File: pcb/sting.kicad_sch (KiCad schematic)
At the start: 100 parts, among them J1 Conn_01x02, SW1 SW_Push, SW10 SW_Push, SW11 SW_Push, SW12 SW_Push, SW13 SW_Push, SW14 SW_Push, SW15 SW_Push, SW16 SW_Push, SW17 SW_Push, SW18 SW_Push, SW19 SW_Push, SW2 SW_Push, SW20 SW_Push, SW21 RotaryEncoder_Switch, SW22 SW_Push, SW23 SW_Push, SW24 SW_Push, SW25 SW_Push, SW26 SW_Push, SW27 SW_Push, SW28 SW_Push, SW29 SW_Push, SW3 SW_Push, SW30 SW_Push, SW31 SW_Push, SW32 SW_Push, SW33 SW_Push, SW34 SW_Push, SW35 SW_Push, SW36 SW_Push, SW37 SW_Push, SW38 SW_Push, SW39 SW_Push, SW4 SW_Push, SW40 SW_Push, SW41 SW_Push, SW42 SW_Push, SW43 SW_Push, SW44 SW_Push, SW45 SW_Push, SW46 SW_Push, SW48 SW_Push, SW49 SW_Push, SW5 SW_Push, SW6 SW_Push, SW7 SW_Push, SW8 SW_Push, SW9 SW_Push, U1 nice_nano

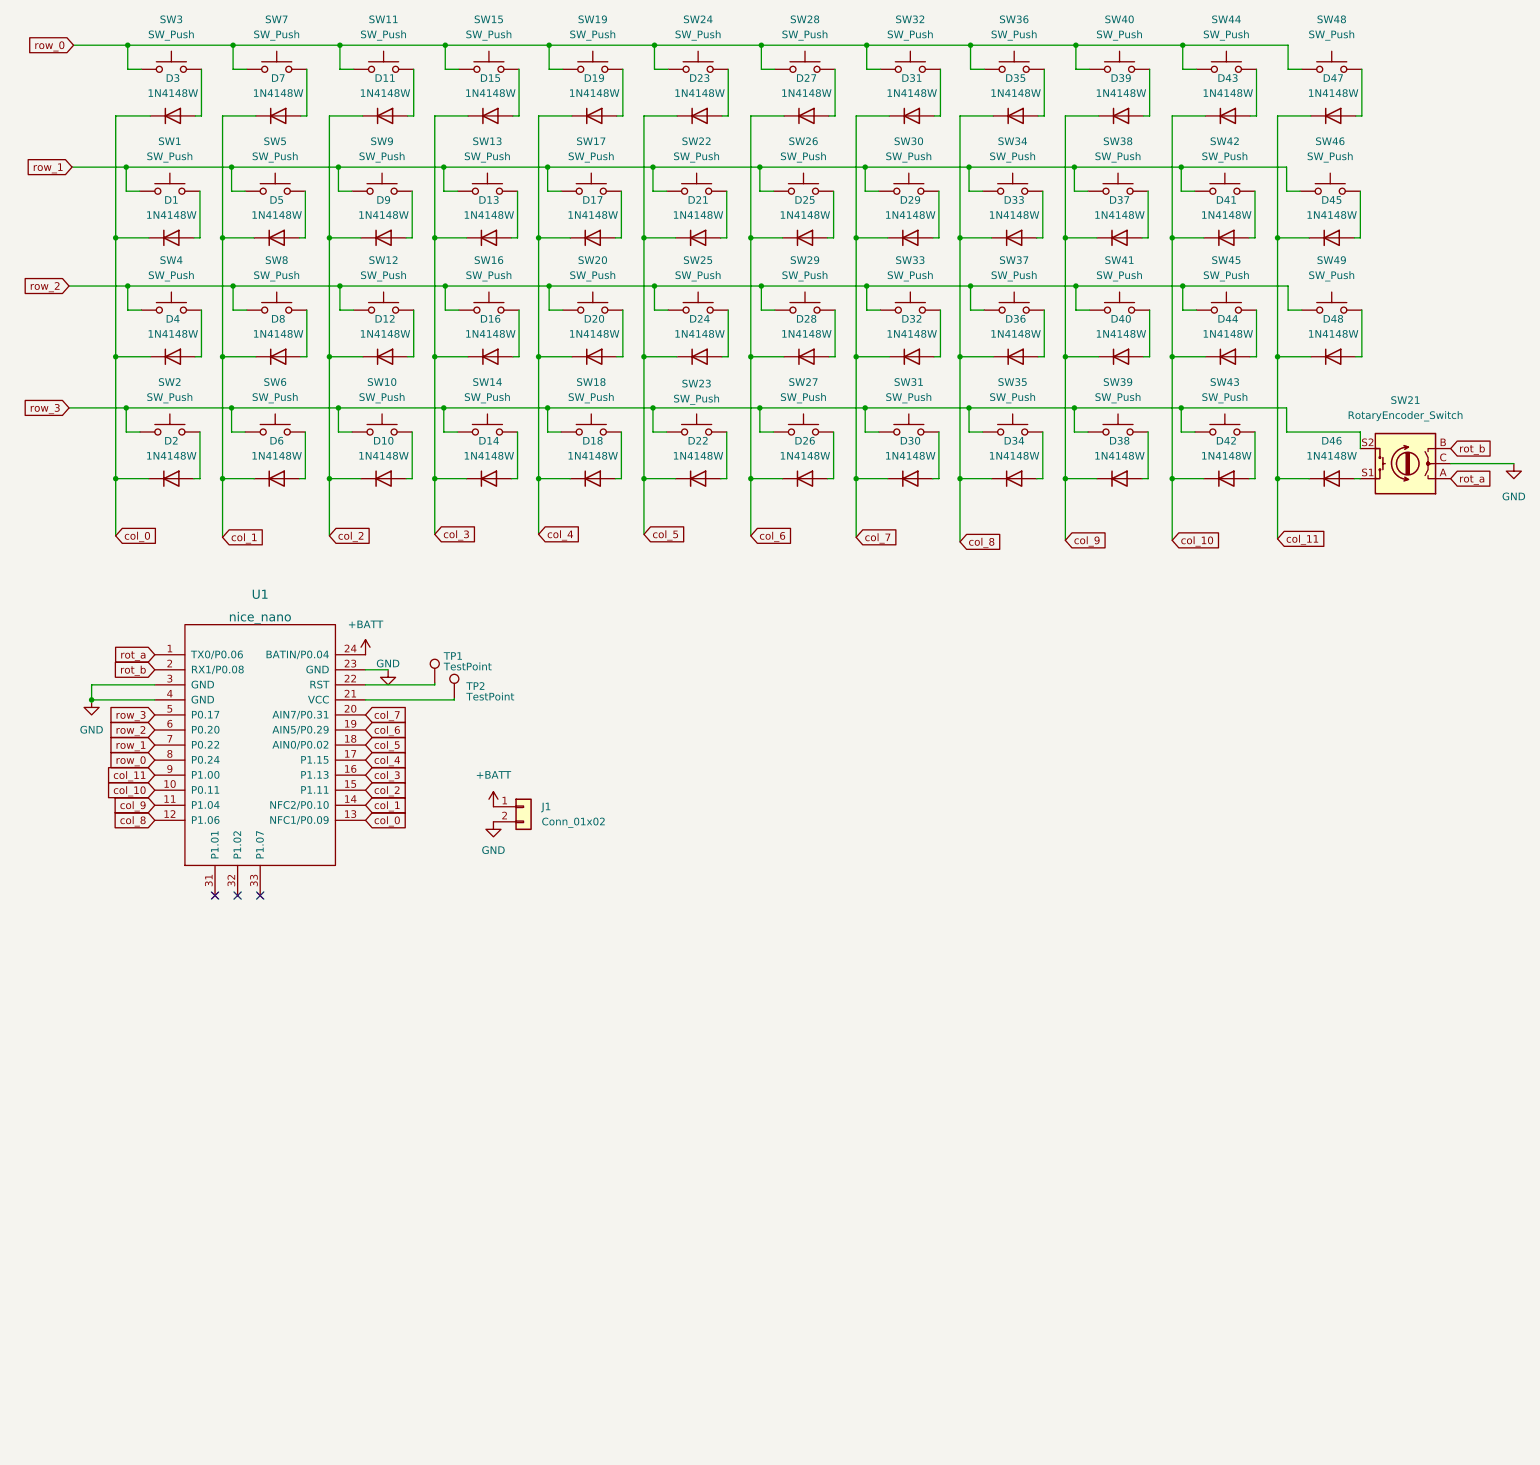
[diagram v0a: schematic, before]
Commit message: change key matrix and add encoder to schematic
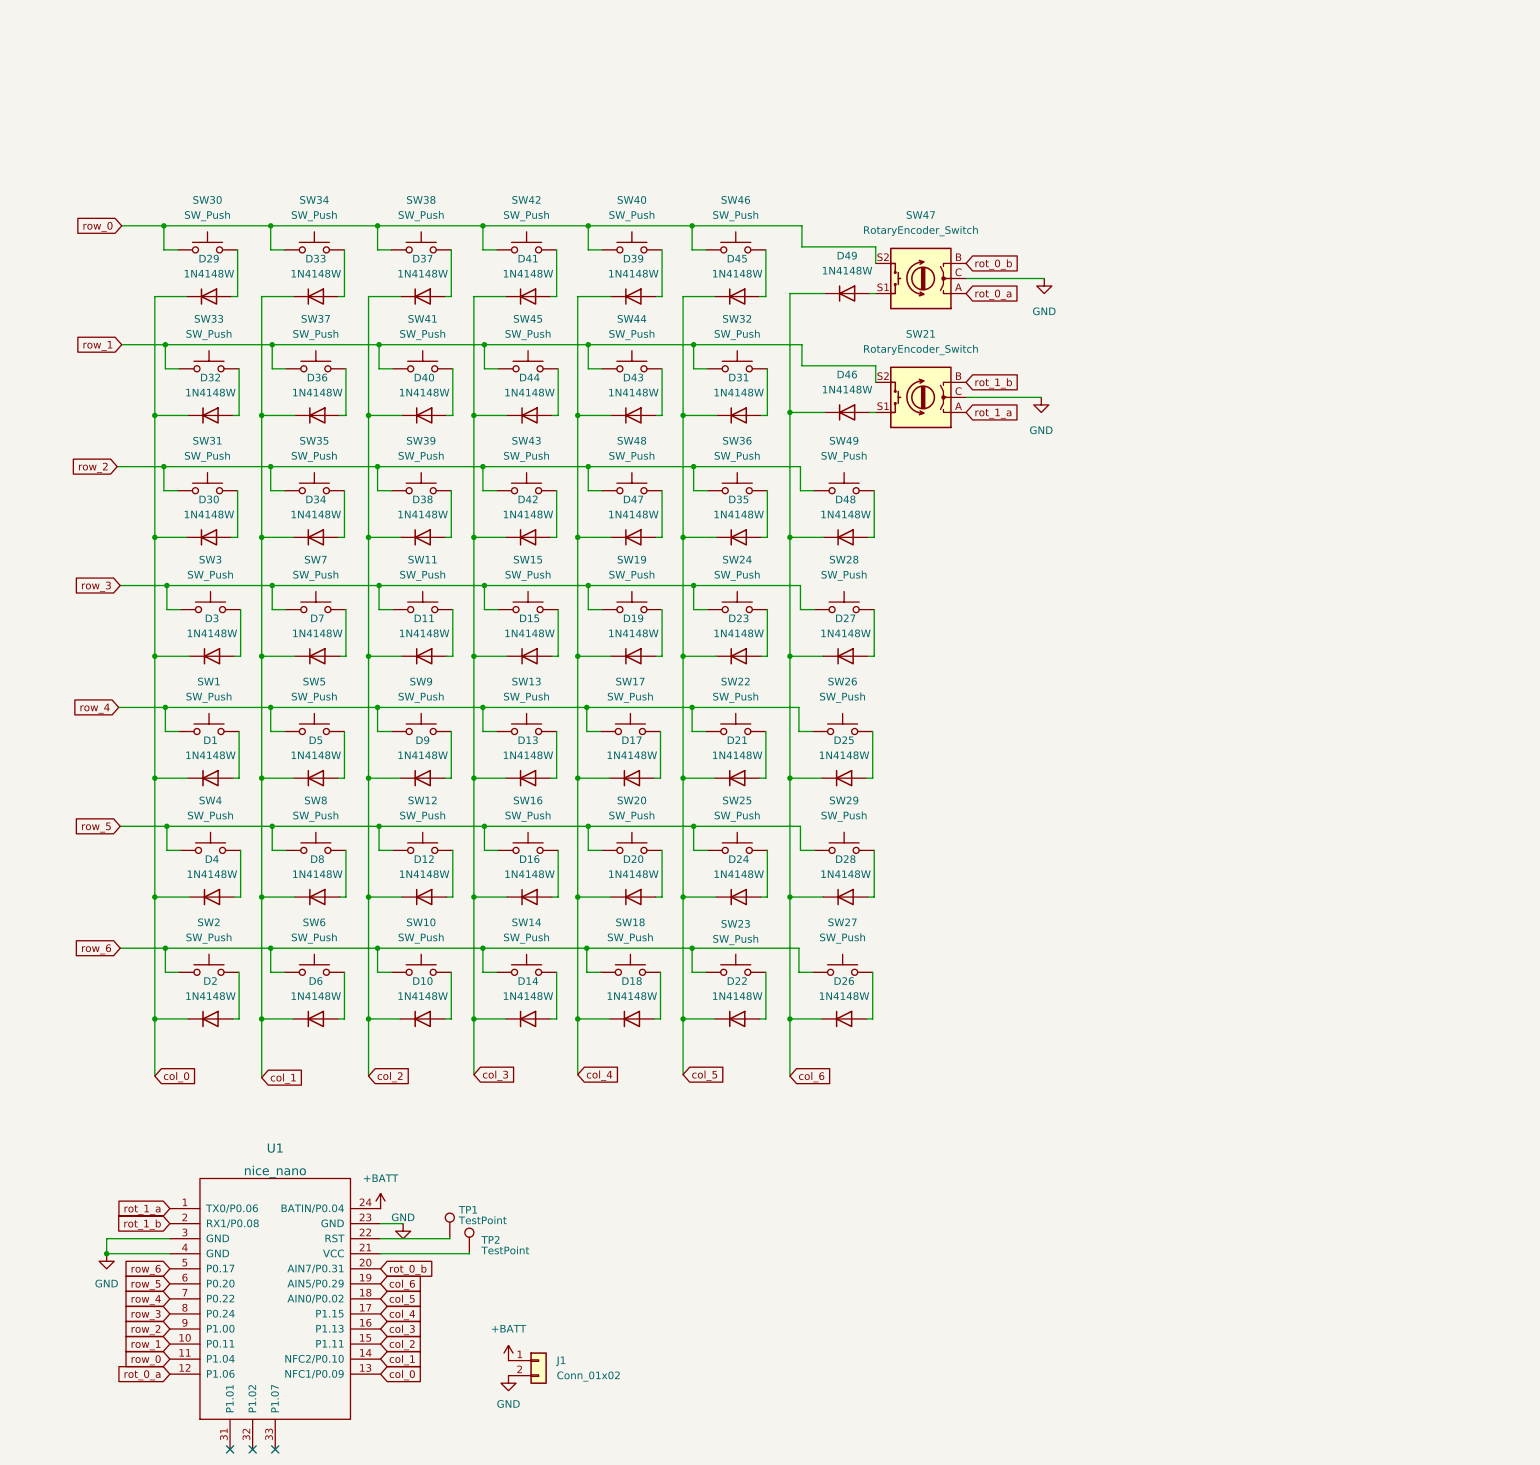
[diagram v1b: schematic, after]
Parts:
- added D49: 1N4148W, Diode_SMD:D_SOD-123, symbol Diode:1N4148W
- added SW47: RotaryEncoder_Switch, foostan:RotaryEncoder_EC12-SW, symbol Device:RotaryEncoder_Switch
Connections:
- net GND: now also SW47.C
- net col_0: now also D29.1 (K), D30.1 (K), D32.1 (K)
- net col_1: now also D33.1 (K), D34.1 (K), D36.1 (K)
- net col_2: now also D37.1 (K), D38.1 (K), D40.1 (K)
- net col_3: now also D41.1 (K), D42.1 (K), D44.1 (K)
- net col_4: now also D39.1 (K), D43.1 (K), D47.1 (K)
- net col_5: now also D31.1 (K), D35.1 (K), D45.1 (K)
- net col_6: now also D46.1 (K), D48.1 (K), D49.1 (K)
- net row_0: now also SW30.1, SW34.1, SW38.1, SW42.1, SW46.1, U1.11 (P1.04), SW47.S2; no longer SW11.1, SW15.1, SW19.1, SW24.1, SW28.1, SW3.1, SW32.1, SW36.1, SW44.1, SW48.1, SW7.1, U1.8 (P0.24)
- net row_1: now also SW21.S2, SW32.1, SW33.1, SW37.1, SW41.1, SW44.1, SW45.1, U1.10 (P0.11); no longer SW1.1, SW13.1, SW17.1, SW22.1, SW26.1, SW30.1, SW34.1, SW38.1, SW42.1, SW46.1, SW5.1, SW9.1, U1.7 (P0.22)
- net row_2: now also SW31.1, SW35.1, SW36.1, SW39.1, SW43.1, SW48.1, U1.9 (P1.00); no longer SW12.1, SW16.1, SW20.1, SW25.1, SW29.1, SW33.1, SW37.1, SW4.1, SW41.1, SW45.1, SW8.1, U1.6 (P0.20)
- net row_3: now also SW11.1, SW15.1, SW19.1, SW24.1, SW28.1, SW3.1, SW7.1, U1.8 (P0.24); no longer SW10.1, SW14.1, SW18.1, SW2.1, SW21.S2, SW23.1, SW27.1, SW31.1, SW35.1, SW39.1, SW43.1, SW6.1, U1.5 (P0.17)
- removed net col_10: D41.1 (K), D42.1 (K), D43.1 (K), D44.1 (K), U1.10 (P0.11)
- removed net col_11: D45.1 (K), D46.1 (K), D47.1 (K), D48.1 (K), U1.9 (P1.00)
- removed net col_7: D29.1 (K), D30.1 (K), D31.1 (K), D32.1 (K), U1.20 (AIN7/P0.31)
- removed net col_8: D33.1 (K), D34.1 (K), D35.1 (K), D36.1 (K), U1.12 (P1.06)
- removed net col_9: D37.1 (K), D38.1 (K), D39.1 (K), D40.1 (K), U1.11 (P1.04)
- net rot_a renamed rot_1_a
- net rot_b renamed rot_1_b
- new net: D49.2 (A), SW47.S1
- new net rot_0_a: SW47.A, U1.12 (P1.06)
- new net rot_0_b: SW47.B, U1.20 (AIN7/P0.31)
- new net row_4: SW1.1, SW13.1, SW17.1, SW22.1, SW26.1, SW5.1, SW9.1, U1.7 (P0.22)
- new net row_5: SW12.1, SW16.1, SW20.1, SW25.1, SW29.1, SW4.1, SW8.1, U1.6 (P0.20)
- new net row_6: SW10.1, SW14.1, SW18.1, SW2.1, SW23.1, SW27.1, SW6.1, U1.5 (P0.17)
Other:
- moved on the sheet: D1, D10, D11, D12, D13, D14, D15, D16, D17, D18, D19, D2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
